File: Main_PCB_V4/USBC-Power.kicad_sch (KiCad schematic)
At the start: 24 parts, among them J29 USB_C_Receptacle_USB2.0_16P, U9 FT231XS

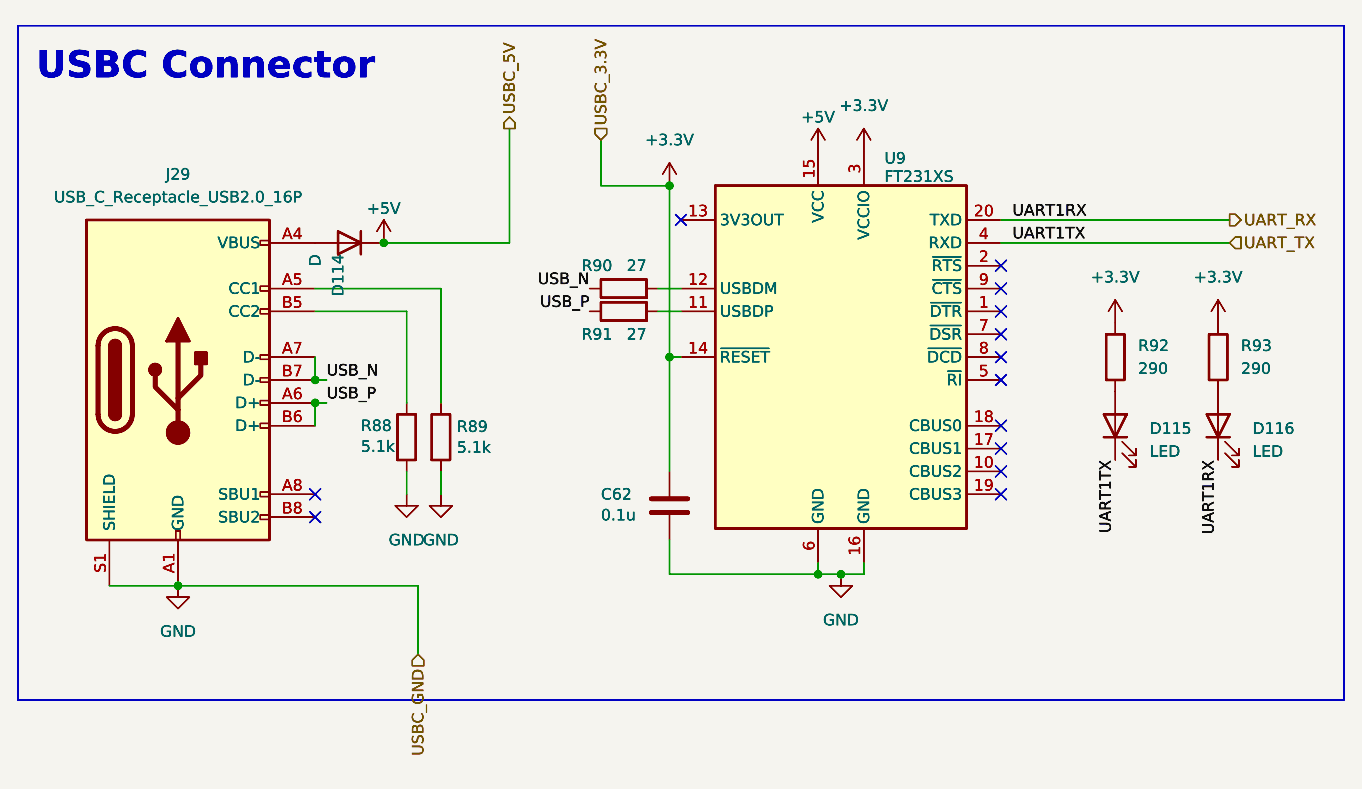
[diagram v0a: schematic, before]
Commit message: Added hierarchy for encoders. Started hierarchy for power.
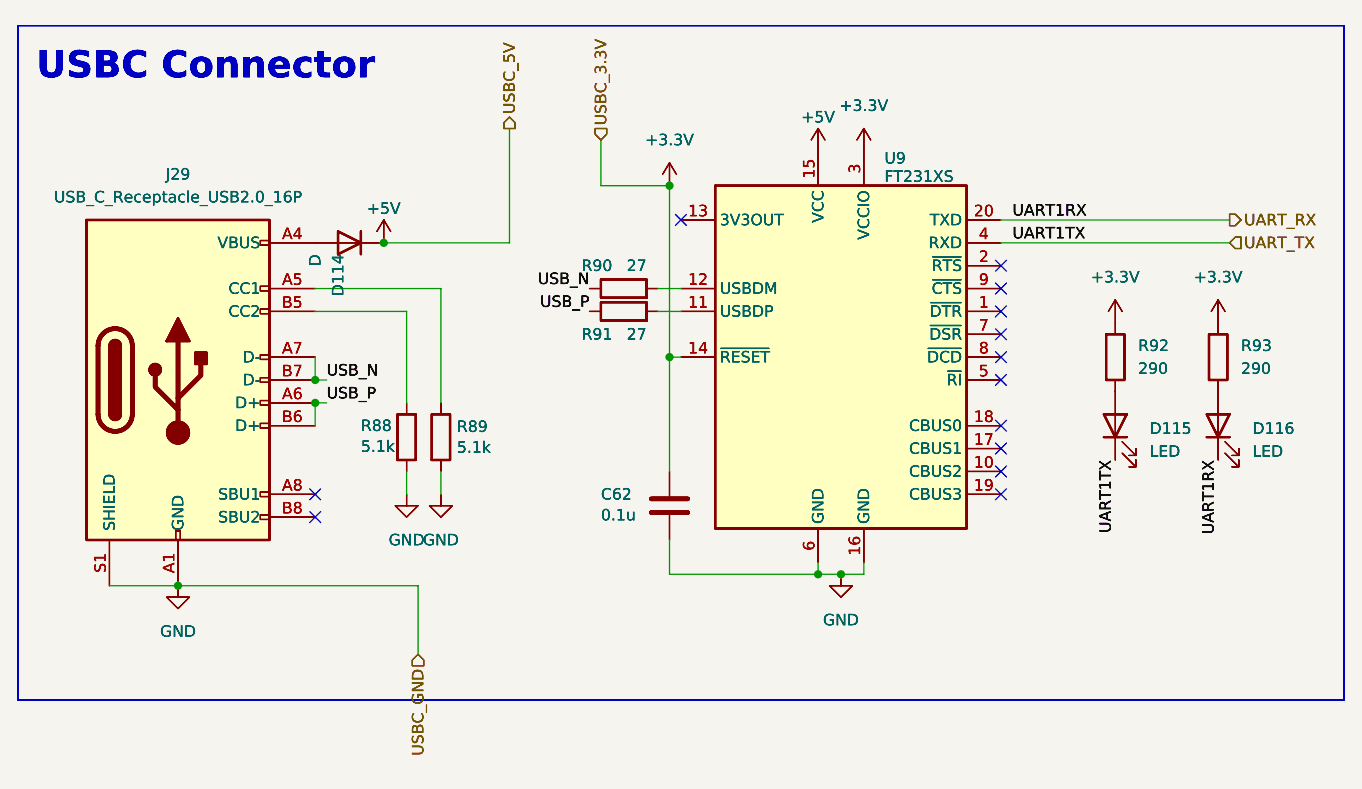
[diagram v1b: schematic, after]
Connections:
- no-connect marks 26 -> 13

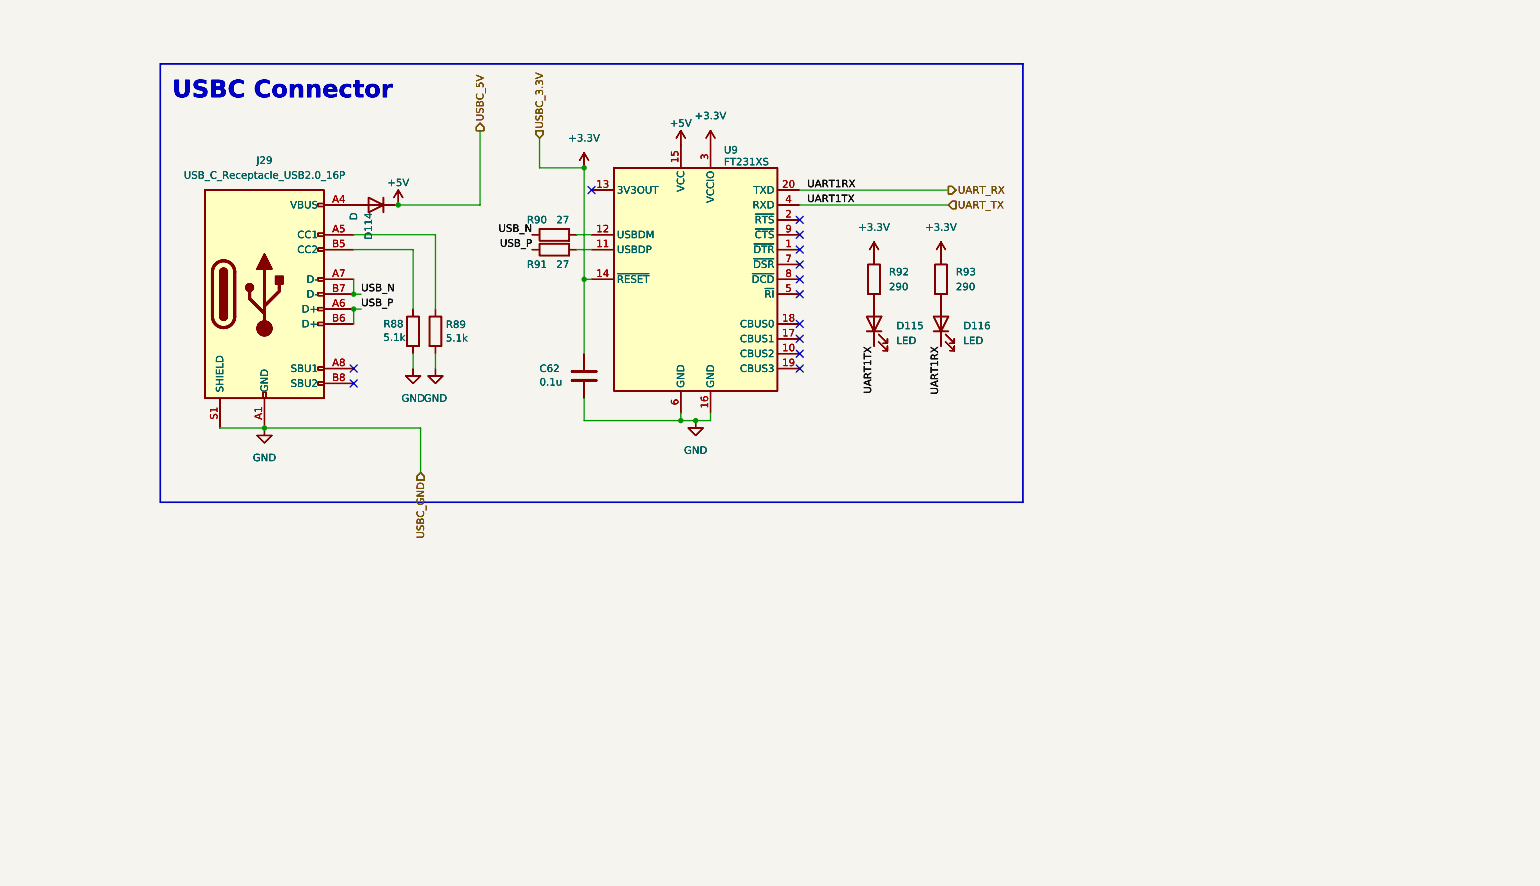
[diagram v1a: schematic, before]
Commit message: moved all power sources to own sheet
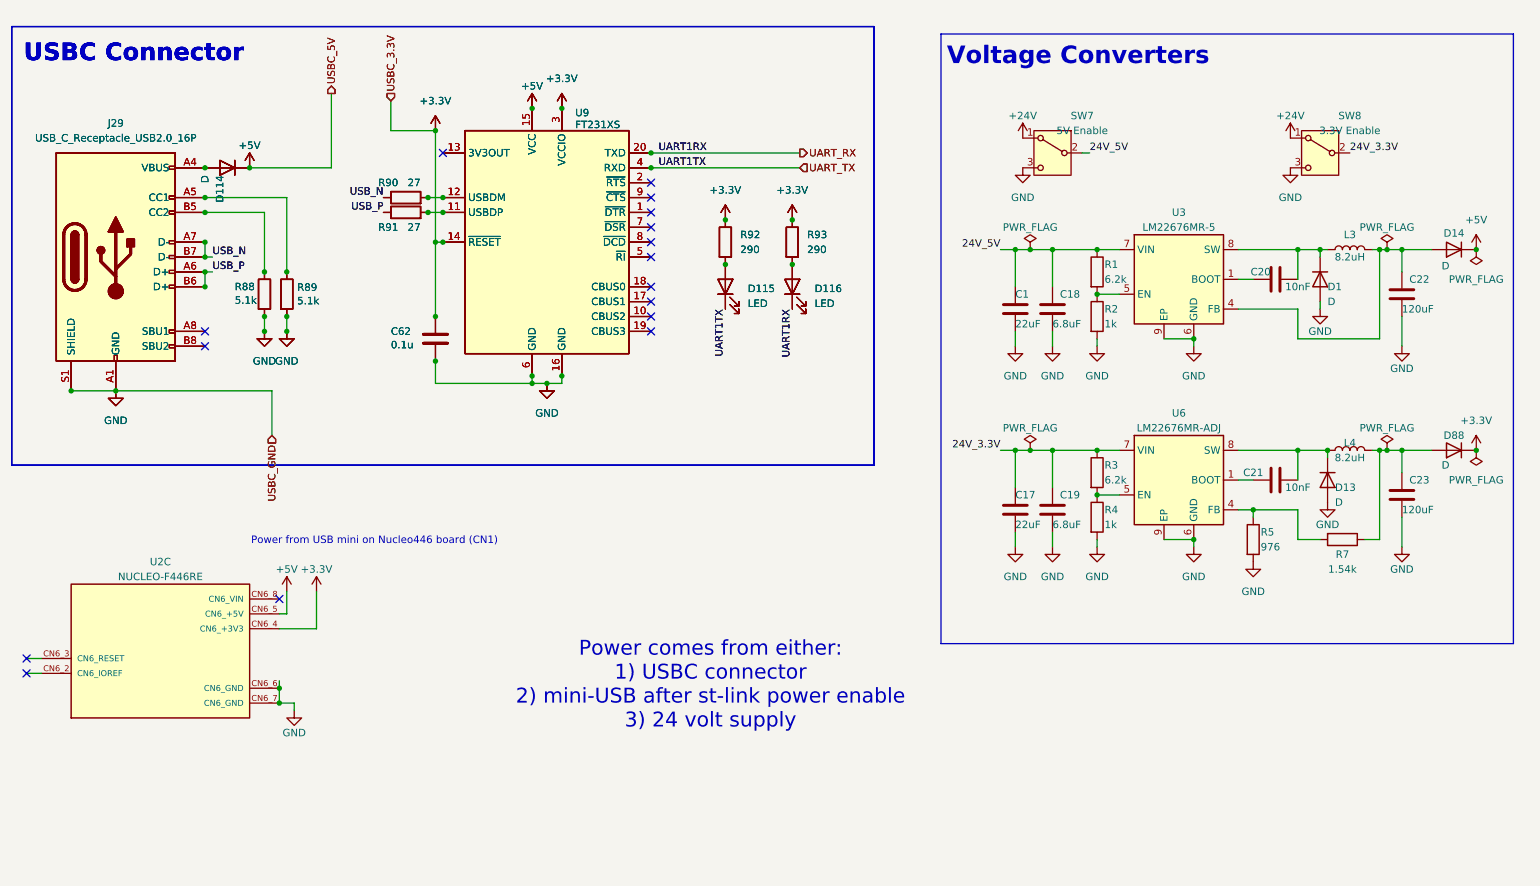
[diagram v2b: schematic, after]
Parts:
- added C1, C17: 22uF, Capacitor_THT:CP_Radial_D5.0mm_P2.00mm, symbol Device:C
- added C18, C19: 6.8uF, Capacitor_SMD:C_0805_2012Metric, symbol Device:C
- added C20, C21: 10nF, Capacitor_SMD:C_0805_2012Metric, symbol Device:C
- added C22, C23: 120uF, Capacitor_THT:CP_Radial_D6.3mm_P2.50mm, symbol Device:C
- added D1, D13, D14, D88: D, Diode_SMD:D_SMA_Handsoldering, symbol Device:D
- added L3, L4: 8.2uH, Inductor_SMD:L_7.3x7.3_H3.5, symbol Device:L
- added R1, R3: 6.2k, Resistor_SMD:R_0805_2012Metric, symbol Device:R
- added R2, R4: 1k, Resistor_SMD:R_0805_2012Metric, symbol Device:R
- added R5: 976, Resistor_SMD:R_0805_2012Metric, symbol Device:R
- added R7: 1.54k, Resistor_SMD:R_0805_2012Metric, symbol Device:R
- added SW7: 5V Enable, Button_Switch_THT:SW_Slide_SPDT_Straight_CK_OS102011MS2Q, symbol Switch:SW_SPDT
- added SW8: 3.3V Enable, Button_Switch_THT:SW_Slide_SPDT_Straight_CK_OS102011MS2Q, symbol Switch:SW_SPDT
- added U2: NUCLEO-F446RE, nucleo446-footprint:MODULE_NUCLEO-F446RE, symbol NUCLEO-F446RE:NUCLEO-F446RE
- added U3: LM22676MR-5, Package_SO:TI_SO-PowerPAD-8, symbol Regulator_Switching:LM22676MR-5
- added U6: LM22676MR-ADJ, Package_SO:TI_SO-PowerPAD-8, symbol Regulator_Switching:LM22676MR-ADJ
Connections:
- net +3.3V: now also D88.1 (K), U2.CN6_4 (CN6_+3V3)
- net +5V: now also D14.1 (K), U2.CN6_5 (CN6_+5V)
- net GND: now also C1.2, C17.2, C18.2, C19.2, C22.2, C23.2, D1.2 (A), D13.2 (A), R2.2, R4.2, R5.2, SW7.3 (C), SW8.3 (C), U2.CN6_6 (CN6_GND), U2.CN6_7 (CN6_GND), U3.6 (GND), U3.9 (EP), U6.6 (GND), U6.9 (EP)
- new net: C21.1, U6.1 (BOOT)
- new net: C21.2, D13.1 (K), L4.1, U6.8 (SW)
- new net: C23.1, D88.2 (A), L4.2, R7.1
- new net: R5.1, R7.2, U6.4 (FB)
- new net: C20.2, D1.1 (K), L3.1, U3.8 (SW)
- new net: C22.1, D14.2 (A), L3.2, U3.4 (FB)
- new net: R1.2, R2.1, U3.5 (EN)
- new net: C20.1, U3.1 (BOOT)
- new net: R3.2, R4.1, U6.5 (EN)
- new net +24V: SW7.1 (A), SW8.1 (A)
- new net 24V_3.3V: C17.1, C19.1, R3.1, SW8.2 (B), U6.7 (VIN)
- new net 24V_5V: C1.1, C18.1, R1.1, SW7.2 (B), U3.7 (VIN)
- no-connect marks 13 -> 16
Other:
- note added: "Power comes from either: 1) USBC connector 2) mini-USB after st-link power enable 3) 24 volt supply"
- note added: "Power from USB mini on Nucleo446 board (CN1)"
- note added: "Voltage Converters"
- moved on the sheet: C62, D114, D115, D116, J29, R88, R89, R90, R91, R92, R93, U9

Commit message: added J9 connector and 5V 3.3V buck converters to schematic
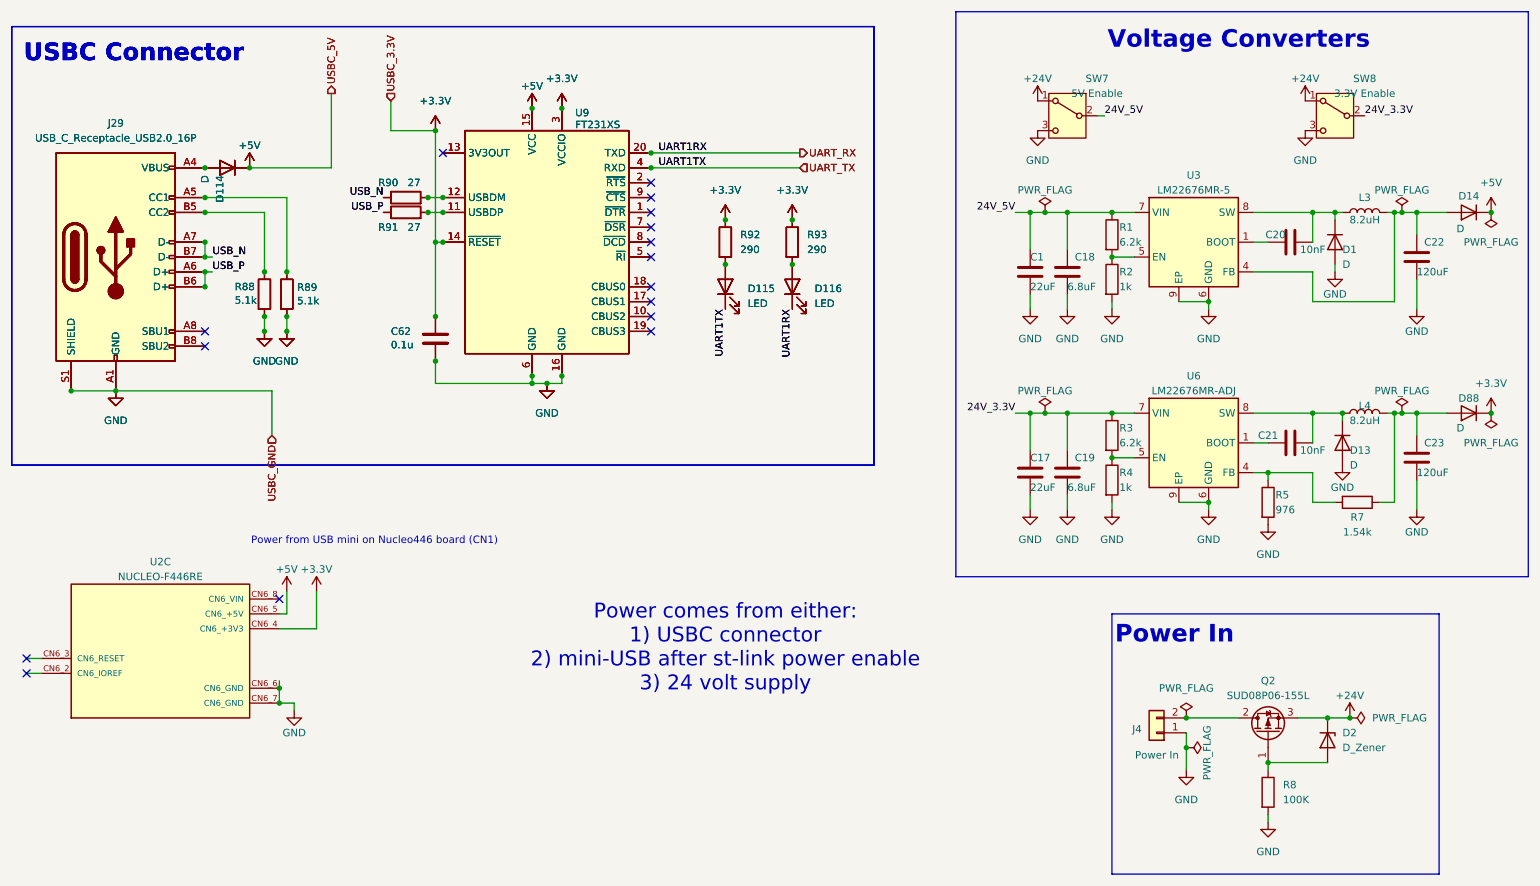
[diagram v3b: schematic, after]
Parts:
- added D2: D_Zener, Diode_SMD:D_SMA_Handsoldering, symbol Device:D_Zener
- added J4: Power In, Connector_AMASS:AMASS_XT60-M_1x02_P7.20mm_Vertical, symbol Connector_Generic:Conn_01x02
- added Q2: SUD08P06-155L, Package_TO_SOT_SMD:TO-252-2, symbol Transistor_FET:SUD08P06-155L
- added R8: 100K, Resistor_SMD:R_0805_2012Metric, symbol Device:R
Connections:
- net +24V: now also D2.1 (K), Q2.3 (S)
- net GND: now also J4.1 (Pin_1), R8.2
- new net: D2.2 (A), Q2.1 (G), R8.1
- new net: J4.2 (Pin_2), Q2.2 (D)
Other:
- note added: "Power In"
- moved on the sheet: C1, C17, C18, C19, C20, C21, C22, C23, D1, D13, D14, D88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
